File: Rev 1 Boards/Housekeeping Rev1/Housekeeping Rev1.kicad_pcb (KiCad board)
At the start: 2 copper layers, 109 x 90 mm, 64 parts, among them J1 Conn_01x02_Socket, J2 Conn_01x02_Socket, J3 Conn_01x02_Socket, J4 Conn_01x02_Socket, J5 Conn_01x02_Socket, J6 Conn_01x02_Socket, U1 MC34063A, U2 MC34063A, U3 MC34063A, U4 MC34063A

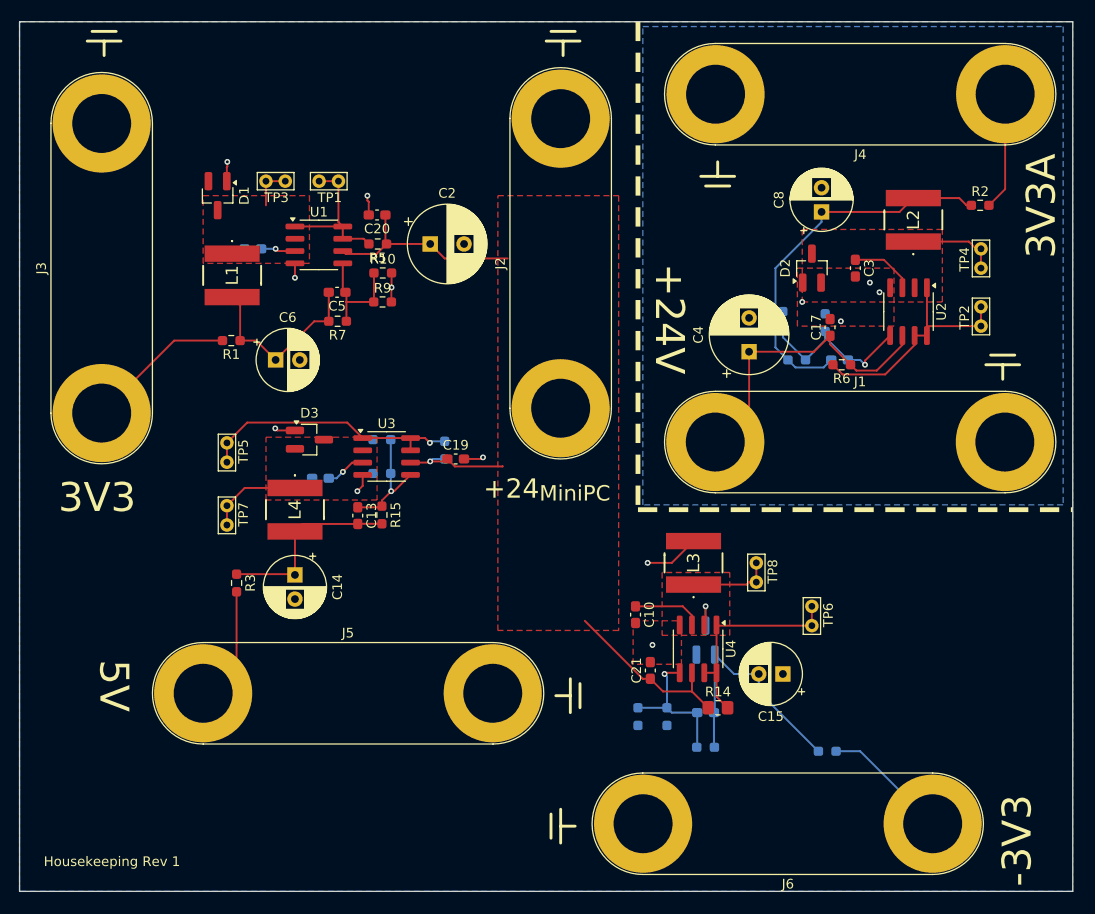
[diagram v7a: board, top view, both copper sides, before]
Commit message: fixed DRC violations with housekeeping PCB layout
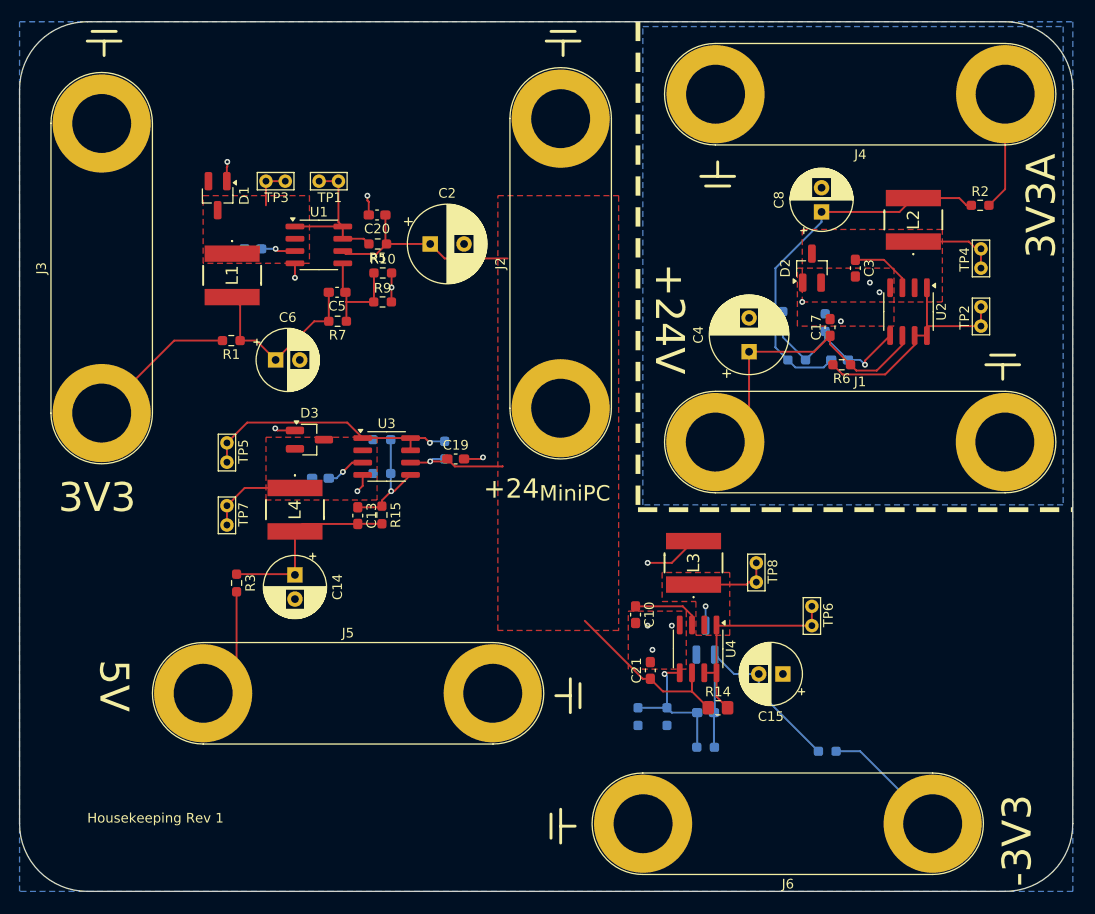
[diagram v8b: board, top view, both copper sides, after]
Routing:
- net /Housekeeping Power Supplies/-3V3_SW: track 12.9 -> 11.2 mm
- net GND: vias 9 -> 11
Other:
- outline, holes or cut-outs redrawn
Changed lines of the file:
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@@
 		(layer "F.SilkS")
 	)
-	(gr_rect
-		(start 147.5 20.5)
-		(end 256.5 110.5)
+	(gr_line
+		(start 256.5 27.5)
+		(end 256.5 103.5)
 		(stroke
 			(width 0.05)
 			(type default)
 		)
-		(fill no)
+		(layer "Edge.Cuts")
+	)
+	(gr_arc
+		(start 249.5 20.5)
+		(mid 254.449747 22.550253)
+		(end 256.5 27.5)
+		(stroke
+			(width 0.05)
+			(type default)
+		)
+		(layer "Edge.Cuts")
+	)
+	(gr_line
+		(start 249.5 110.5)
+		(end 154.5 110.5)
+		(stroke
+			(width 0.05)
+			(type default)
+		)
+		(layer "Edge.Cuts")
+	)
+	(gr_line
+		(start 147.5 103.5)
+		(end 147.5 27.5)
+		(stroke
+			(width 0.05)
+			(type default)
+		)
+		(layer "Edge.Cuts")
+	)
+	(gr_arc
+		(start 154.5 110.5)
+		(mid 149.550253 108.449747)
+		(end 147.5 103.5)
+		(stroke
+			(width 0.05)
+			(type default)
+		)
+		(layer "Edge.Cuts")
+	)
+	(gr_arc
+		(start 256.5 103.5)
+		(mid 254.449747 108.449747)
+		(end 249.5 110.5)
+		(stroke
+			(width 0.05)
+			(type default)
+		)
+		(layer "Edge.Cuts")
+	)
+	(gr_line
+		(start 154.5 20.5)
+		(end 249.5 20.5)
+		(stroke
+			(width 0.05)
+			(type default)
+		)
+		(layer "Edge.Cuts")
+	)
+	(gr_arc
+		(start 147.5 27.5)
+		(mid 149.550253 22.550253)
+		(end 154.5 20.5)
+		(stroke
+			(width 0.05)
+			(type default)
+		)
 		(layer "Edge.Cuts")
 	)
@@
 	)
 	(gr_text "Housekeeping Rev 1\n"
-		(at 150 108 0)
+		(at 154.5 103.5 0)
 		(layer "F.SilkS")
 		(effects
@@
 	)
 	(via
-		(at 213 85)
+		(at 213 85.5)
+		(size 0.6)
+		(drill 0.3)
+		(layers "F.Cu" "B.Cu")
+		(free yes)
+		(net 1)
+	)
+	(via
+		(at 215 83)
+		(size 0.6)
+		(drill 0.3)
+		(layers "F.Cu" "B.Cu")
+		(free yes)
+		(net 1)
+	)
+	(via
+		(at 212.5 83)
 		(size 0.6)
 		(drill 0.3)
@@
 		(start 217.5 78.5)
 		(end 217.25 78.75)
-		(width 0.2)
-		(layer "F.Cu")
-		(net 24)
-	)
-	(segment
-		(start 218.5 81)
-		(end 218.5 82.79)
 		(width 0.2)
 		(layer "F.Cu")
@@
 		(polygon
 			(pts
-				(xy 214 77.5) (xy 214 84) (xy 221 84) (xy 221 77.5)
+				(xy 214 77.5) (xy 214 80.5) (xy 217.5 80.5) (xy 217.5 84) (xy 221 84) (xy 221 77.5)
 			)
 		)
@@
 		(hatch edge 0.5)
 		(priority 4)
-		(connect_pads
+		(connect_pads yes
 			(clearance 0.5)
 		)
@@
 		(polygon
 			(pts
-				(xy 211 82.5) (xy 216 82.5) (xy 216 87) (xy 211 87)
+				(xy 210.5 81.5) (xy 216.5 81.5) (xy 216.5 87.5) (xy 210.5 87.5)
 			)
 		)
